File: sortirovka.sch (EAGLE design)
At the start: 37 parts, among them IC1 DS1307/PCF8583, U1 MAX3485CSA, X1 PI3-CONMINIBOARD, X10 MKDSN1,5/3-5,08, X3 MKDSN1,5/4-5,08, X4 MKDSN1,5/2-5,08, X6 22-23-2051

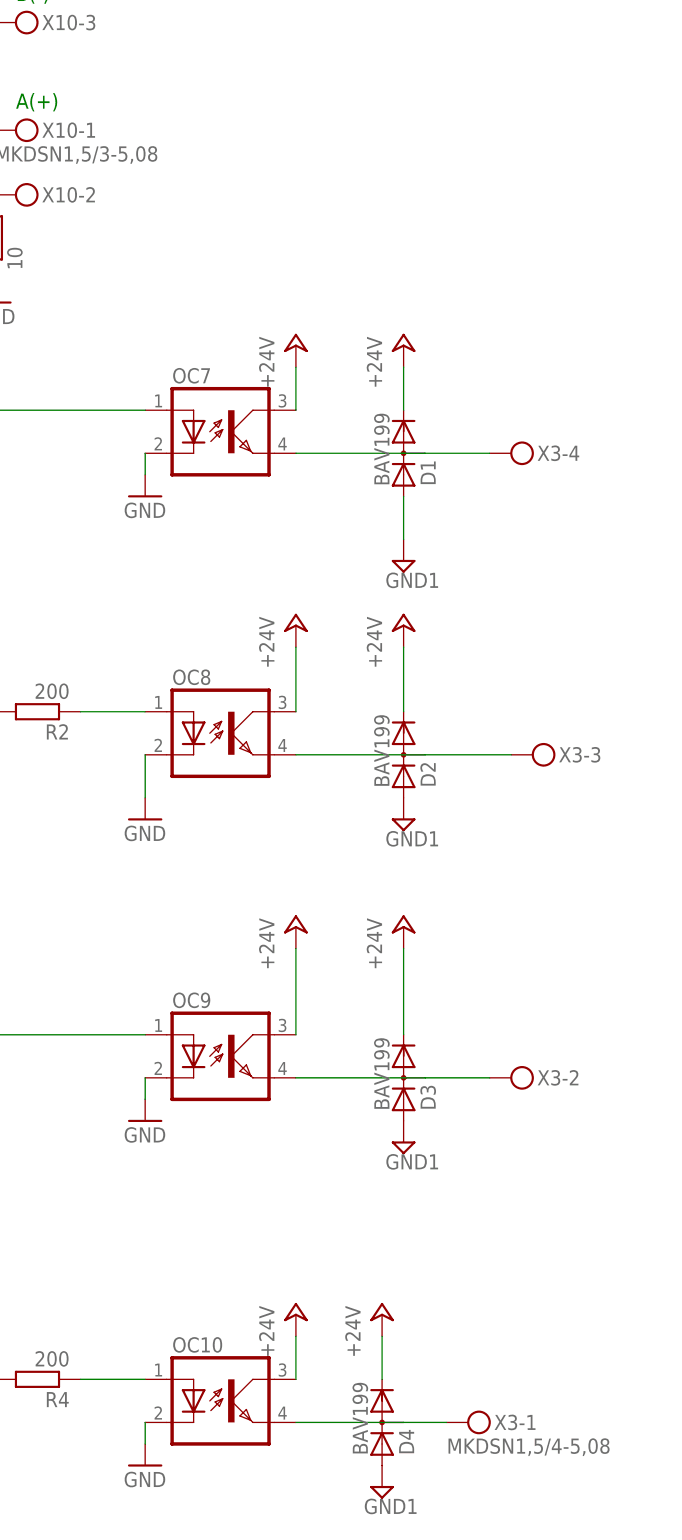
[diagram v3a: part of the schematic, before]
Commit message: current source for optocoupler, old design
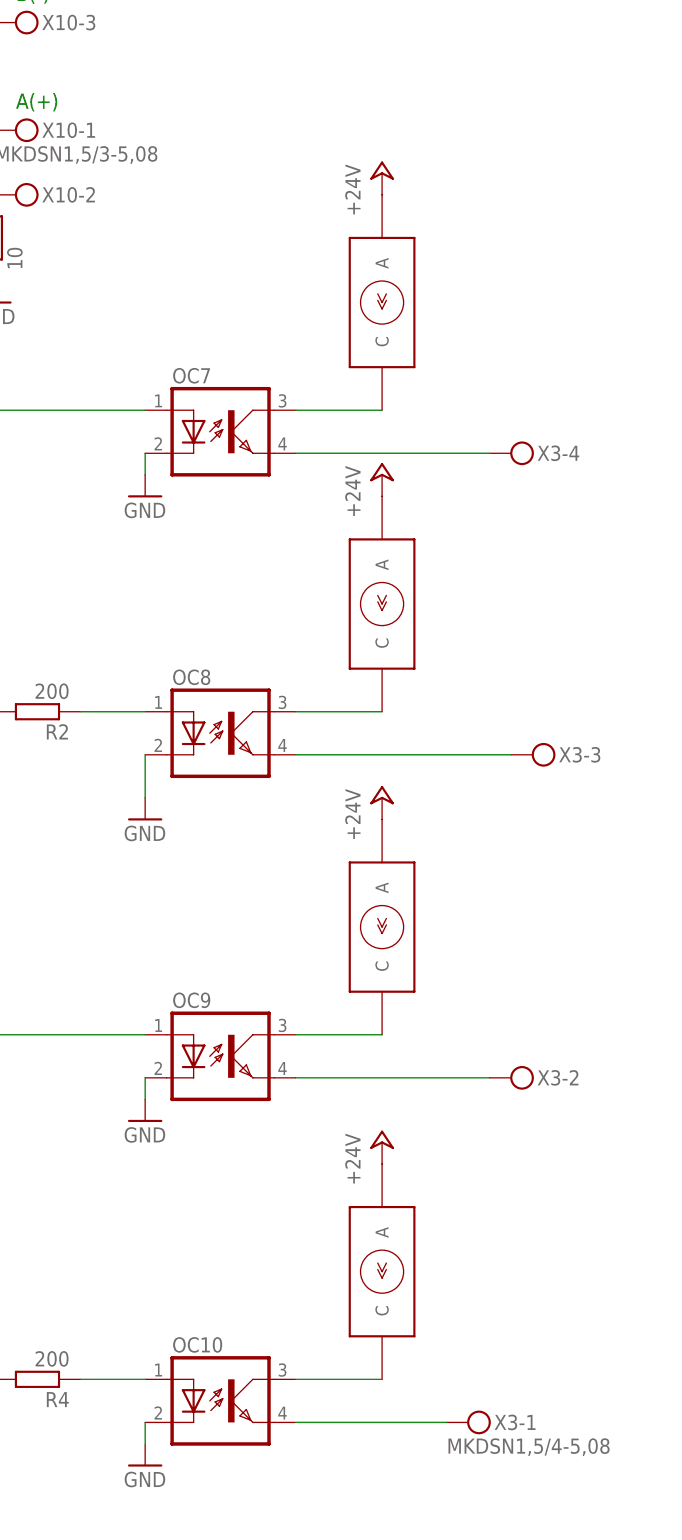
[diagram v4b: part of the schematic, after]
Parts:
- removed D1, D2, D3, D4: BAV199, MyLib:BAV199
- added U$1, U$2, U$4, U$5: NSI45020AT1GSOD-123, MyLib:NSI45020AT1GSOD-123
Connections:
- new net N$14: OC10.COL, U$5.C
- new net N$17: OC9.COL, U$1.C
- new net N$20: OC8.COL, U$4.C
- new net N$30: OC7.COL, U$2.C
- net +24V: now also U$1.A, U$2.A, U$4.A, U$5.A; no longer D1.C, D2.C, D3.C, D4.C, OC10.COL, OC7.COL, OC8.COL, OC9.COL
- net GND1: no longer D1.A, D2.A, D3.A, D4.A
- net N$10: no longer D4.AC
- net N$11: no longer D3.AC
- net N$12: no longer D2.AC
- net N$9: no longer D1.AC
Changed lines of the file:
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@@
 <part name="X4" library="con-phoenix-508" deviceset="MKDSN1,5/2-5,08" device=""/>
 <part name="P+2" library="supply1" deviceset="+24V" device=""/>
-<part name="SUPPLY1" library="supply2" deviceset="GND1" device=""/>
 <part name="SUPPLY5" library="supply2" deviceset="GND1" device=""/>
 <part name="OC7" library="MyLib" deviceset="SFH6106" device="REAL"/>
@@
 <part name="+3V6" library="supply1" deviceset="+3V3" device=""/>
 <part name="PWS1" library="MyLib" deviceset="TEN_3*" device="-1" technology="2410"/>
-<part name="D1" library="MyLib" deviceset="BAV199" device=""/>
-<part name="D2" library="MyLib" deviceset="BAV199" device=""/>
-<part name="D3" library="MyLib" deviceset="BAV199" device=""/>
-<part name="D4" library="MyLib" deviceset="BAV199" device=""/>
-<part name="P+1" library="supply1" deviceset="+24V" device=""/>
-<part name="P+7" library="supply1" deviceset="+24V" device=""/>
-<part name="P+8" library="supply1" deviceset="+24V" device=""/>
-<part name="P+9" library="supply1" deviceset="+24V" device=""/>
-<part name="SUPPLY2" library="supply2" deviceset="GND1" device=""/>
-<part name="SUPPLY3" library="supply2" deviceset="GND1" device=""/>
-<part name="SUPPLY4" library="supply2" deviceset="GND1" device=""/>
+<part name="U$1" library="MyLib" deviceset="NSI45020AT1G" device="SOD-123"/>
+<part name="U$2" library="MyLib" deviceset="NSI45020AT1G" device="SOD-123"/>
+<part name="U$4" library="MyLib" deviceset="NSI45020AT1G" device="SOD-123"/>
+<part name="U$5" library="MyLib" deviceset="NSI45020AT1G" device="SOD-123"/>
 </parts>
 <sheets>
@@
 <instance part="X4" gate="-2" x="147.32" y="144.78" rot="MR0"/>
 <instance part="P+2" gate="1" x="154.94" y="147.32" rot="MR0"/>
-<instance part="SUPPLY1" gate="G$1" x="345.44" y="10.16"/>
 <instance part="SUPPLY5" gate="G$1" x="167.64" y="129.54" rot="MR0"/>
 <instance part="OC7" gate="A" x="325.12" y="25.4"/>
 <instance part="GND2" gate="1" x="314.96" y="17.78"/>
-<instance part="P+3" gate="1" x="332.74" y="35.56"/>
+<instance part="P+3" gate="1" x="342.9" y="55.88"/>
 <instance part="OC8" gate="A" x="325.12" y="-10.16"/>
 <instance part="GND9" gate="1" x="314.96" y="-20.32"/>
-<instance part="P+4" gate="1" x="332.74" y="2.54"/>
+<instance part="P+4" gate="1" x="342.9" y="20.32"/>
 <instance part="OC9" gate="A" x="325.12" y="-48.26"/>
 <instance part="GND12" gate="1" x="314.96" y="-55.88"/>
-<instance part="P+5" gate="1" x="332.74" y="-33.02"/>
+<instance part="P+5" gate="1" x="342.9" y="-17.78"/>
 <instance part="OC10" gate="A" x="325.12" y="-88.9"/>
 <instance part="GND13" gate="1" x="314.96" y="-96.52"/>
-<instance part="P+6" gate="1" x="332.74" y="-78.74"/>
+<instance part="P+6" gate="1" x="342.9" y="-58.42"/>
 <instance part="GND24" gate="1" x="299.72" y="124.46"/>
 <instance part="C8" gate="G$1" x="279.4" y="132.08"/>
@@
 <instance part="+3V6" gate="G$1" x="68.58" y="81.28"/>
 <instance part="PWS1" gate="G$1" x="213.36" y="134.62"/>
-<instance part="D1" gate="G$1" x="345.44" y="22.86" rot="R270"/>
-<instance part="D2" gate="G$1" x="345.44" y="-12.7" rot="R270"/>
-<instance part="D3" gate="G$1" x="345.44" y="-50.8" rot="R270"/>
-<instance part="D4" gate="G$1" x="342.9" y="-91.44" rot="R270"/>
-<instance part="P+1" gate="1" x="342.9" y="-78.74"/>
-<instance part="P+7" gate="1" x="345.44" y="-33.02"/>
-<instance part="P+8" gate="1" x="345.44" y="2.54"/>
-<instance part="P+9" gate="1" x="345.44" y="35.56"/>
-<instance part="SUPPLY2" gate="G$1" x="345.44" y="-20.32"/>
-<instance part="SUPPLY3" gate="G$1" x="342.9" y="-99.06"/>
-<instance part="SUPPLY4" gate="G$1" x="345.44" y="-58.42"/>
+<instance part="U$1" gate="G$1" x="342.9" y="-33.02" rot="R270"/>
+<instance part="U$2" gate="G$1" x="342.9" y="40.64" rot="R270"/>
+<instance part="U$4" gate="G$1" x="342.9" y="5.08" rot="R270"/>
+<instance part="U$5" gate="G$1" x="342.9" y="-73.66" rot="R270"/>
 </instances>
 <busses>
@@
 <pinref part="OC10" gate="A" pin="EMIT"/>
 <pinref part="X3" gate="-1" pin="KL"/>
-<pinref part="D4" gate="G$1" pin="AC"/>
-<wire x1="350.52" y1="-91.44" x2="345.44" y2="-91.44" width="0.1524" layer="91"/>
-<wire x1="345.44" y1="-91.44" x2="332.74" y2="-91.44" width="0.1524" layer="91"/>
+<wire x1="350.52" y1="-91.44" x2="332.74" y2="-91.44" width="0.1524" layer="91"/>
 </segment>
 </net>
@@
 <pinref part="OC8" gate="A" pin="EMIT"/>
 <pinref part="X3" gate="-3" pin="KL"/>
-<pinref part="D2" gate="G$1" pin="AC"/>
-<wire x1="358.14" y1="-12.7" x2="347.98" y2="-12.7" width="0.1524" layer="91"/>
-<wire x1="347.98" y1="-12.7" x2="332.74" y2="-12.7" width="0.1524" layer="91"/>
+<wire x1="358.14" y1="-12.7" x2="332.74" y2="-12.7" width="0.1524" layer="91"/>
 </segment>
 </net>
@@
 </segment>
 <segment>
-<pinref part="OC7" gate="A" pin="COL"/>
+<pinref part="U$5" gate="G$1" pin="A"/>
+<pinref part="P+6" gate="1" pin="+24V"/>
+</segment>
+<segment>
+<pinref part="U$1" gate="G$1" pin="A"/>
+<pinref part="P+5" gate="1" pin="+24V"/>
+</segment>
+<segment>
+<pinref part="U$4" gate="G$1" pin="A"/>
+<pinref part="P+4" gate="1" pin="+24V"/>
+</segment>
+<segment>
+<pinref part="U$2" gate="G$1" pin="A"/>
 <pinref part="P+3" gate="1" pin="+24V"/>
-<wire x1="332.74" y1="27.94" x2="332.74" y2="33.02" width="0.1524" layer="91"/>
-</segment>
-<segment>
-<pinref part="OC8" gate="A" pin="COL"/>
-<pinref part="P+4" gate="1" pin="+24V"/>
-<wire x1="332.74" y1="-7.62" x2="332.74" y2="0" width="0.1524" layer="91"/>
-</segment>
-<segment>
-<pinref part="OC9" gate="A" pin="COL"/>
-<wire x1="332.74" y1="-45.72" x2="332.74" y2="-35.56" width="0.1524" layer="91"/>
-<pinref part="P+5" gate="1" pin="+24V"/>
-</segment>
-<segment>
-<pinref part="OC10" gate="A" pin="COL"/>
-<wire x1="332.74" y1="-86.36" x2="332.74" y2="-81.28" width="0.1524" layer="91"/>
-<pinref part="P+6" gate="1" pin="+24V"/>
-</segment>
-<segment>
-<pinref part="D4" gate="G$1" pin="C"/>
-<pinref part="P+1" gate="1" pin="+24V"/>
-<wire x1="342.9" y1="-86.36" x2="342.9" y2="-81.28" width="0.1524" layer="91"/>
-</segment>
-<segment>
-<pinref part="D3" gate="G$1" pin="C"/>
-<pinref part="P+7" gate="1" pin="+24V"/>
-<wire x1="345.44" y1="-45.72" x2="345.44" y2="-35.56" width="0.1524" layer="91"/>
-</segment>
-<segment>
-<pinref part="D2" gate="G$1" pin="C"/>
-<pinref part="P+8" gate="1" pin="+24V"/>
-<wire x1="345.44" y1="-7.62" x2="345.44" y2="0" width="0.1524" layer="91"/>
-</segment>
-<segment>
-<pinref part="D1" gate="G$1" pin="C"/>
-<pinref part="P+9" gate="1" pin="+24V"/>
-<wire x1="345.44" y1="27.94" x2="345.44" y2="33.02" width="0.1524" layer="91"/>
 </segment>
 </net>
@@
 <junction x="193.04" y="129.54"/>
 </segment>
-<segment>
-<pinref part="D3" gate="G$1" pin="A"/>
-<pinref part="SUPPLY4" gate="G$1" pin="GND1"/>
-</segment>
-<segment>
-<pinref part="D4" gate="G$1" pin="A"/>
-<pinref part="SUPPLY3" gate="G$1" pin="GND1"/>
-</segment>
-<segment>
-<pinref part="D2" gate="G$1" pin="A"/>
-<pinref part="SUPPLY2" gate="G$1" pin="GND1"/>
-</segment>
-<segment>
-<pinref part="D1" gate="G$1" pin="A"/>
-<pinref part="SUPPLY1" gate="G$1" pin="GND1"/>
-<wire x1="345.44" y1="17.78" x2="345.44" y2="12.7" width="0.1524" layer="91"/>
-</segment>
 </net>
 <net name="N$15" class="0">
@@
 <segment>
 <pinref part="X3" gate="-4" pin="KL"/>
-<pinref part="D1" gate="G$1" pin="AC"/>
-<wire x1="355.6" y1="22.86" x2="347.98" y2="22.86" width="0.1524" layer="91"/>
 <pinref part="OC7" gate="A" pin="EMIT"/>
-<wire x1="347.98" y1="22.86" x2="332.74" y2="22.86" width="0.1524" layer="91"/>
+<wire x1="355.6" y1="22.86" x2="332.74" y2="22.86" width="0.1524" layer="91"/>
 </segment>
 </net>
@@
 <segment>
 <pinref part="X3" gate="-2" pin="KL"/>
-<pinref part="D3" gate="G$1" pin="AC"/>
-<wire x1="355.6" y1="-50.8" x2="347.98" y2="-50.8" width="0.1524" layer="91"/>
 <pinref part="OC9" gate="A" pin="EMIT"/>
-<wire x1="347.98" y1="-50.8" x2="332.74" y2="-50.8" width="0.1524" layer="91"/>
+<wire x1="355.6" y1="-50.8" x2="332.74" y2="-50.8" width="0.1524" layer="91"/>
 </segment>
 </net>
@@
 </segment>
 </net>
+<net name="N$14" class="0">
+<segment>
+<pinref part="OC10" gate="A" pin="COL"/>
+<pinref part="U$5" gate="G$1" pin="C"/>
+<wire x1="332.74" y1="-86.36" x2="342.9" y2="-86.36" width="0.1524" layer="91"/>
+</segment>
+</net>
+<net name="N$17" class="0">
+<segment>
+<pinref part="OC9" gate="A" pin="COL"/>
+<pinref part="U$1" gate="G$1" pin="C"/>
+<wire x1="332.74" y1="-45.72" x2="342.9" y2="-45.72" width="0.1524" layer="91"/>
+</segment>
+</net>
+<net name="N$20" class="0">
+<segment>
+<pinref part="OC8" gate="A" pin="COL"/>
+<pinref part="U$4" gate="G$1" pin="C"/>
+<wire x1="332.74" y1="-7.62" x2="342.9" y2="-7.62" width="0.1524" layer="91"/>
+</segment>
+</net>
+<net name="N$30" class="0">
+<segment>
+<pinref part="OC7" gate="A" pin="COL"/>
+<pinref part="U$2" gate="G$1" pin="C"/>
+<wire x1="332.74" y1="27.94" x2="342.9" y2="27.94" width="0.1524" layer="91"/>
+</segment>
+</net>

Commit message: wip
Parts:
- removed R15: 120, rcl:R-EU_0207/10
- removed X10: MKDSN1,5/3-5,08, con-phoenix-508:MKDSN1,5/3-5,08
- removed X6: 22-23-2051, con-molex:22-23-2051
- added IC2: PCF8574T, MyLib:PCF8574T
- added IC3: DS1307/PCF8583, MyLib:DS1307/PCF8583
- added LCD1: LCD_2X16_SIL, lcd_2x16_led_backlight:LCD_2X16_SIL
- added LCD2: LCD_128X64-NO_RESTRICTS, lcd_128x64_led_backlight:LCD_128X64-NO_RESTRICTS
- added R12: 200, rcl:R-EU_R0805
- added X2: PI3-CONMINIBOARD, MyLib:PI3-CONMINIBOARD
- added X5: MKDSN1,5/4-5,08, con-phoenix-508:MKDSN1,5/4-5,08
- IC1: value DS1307/PCF8583 -> PCF8574T; device MyLib:DS1307/PCF8583 -> MyLib:PCF8574T
- R1, R2: value 200 -> 3k3
- R10: value 3k3 -> 10
- R11: value 3k3 -> 200
- R3, R4: value 200 -> 1k5
- R5, R6: value 1k5 -> 15
- R7: value 15 -> 200
- R8: value 15 -> 120; device rcl:R-EU_R0805 -> rcl:R-EU_0207/10
- R9: value 10 -> 200
- X1: value PI3-CONMINIBOARD -> 22-23-2051; device MyLib:PI3-CONMINIBOARD -> con-molex:22-23-2051
- X3: value MKDSN1,5/4-5,08 -> MKDSN1,5/2-5,08; device con-phoenix-508:MKDSN1,5/4-5,08 -> con-phoenix-508:MKDSN1,5/2-5,08
- X4: value MKDSN1,5/2-5,08 -> MKDSN1,5/3-5,08; device con-phoenix-508:MKDSN1,5/2-5,08 -> con-phoenix-508:MKDSN1,5/3-5,08
- renumbered C10 to C2, C8 to C4, C9 to C3, OC10 to OC4, OC7 to OC1, OC8 to OC2, OC9 to OC3, U$1 to D4, U$2 to D2, U$3 to D1, U$4 to D3, U$5 to D5
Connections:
- net +24V: now also X3-2.KL; no longer X4-2.KL
- net +3V3: now also IC1.A0, IC1.VDD, IC2.VDD, IC3.VCC, R1.2, R2.2, R4.1, X2.3.3V@1, X2.3.3V@2; no longer IC1.VCC, R10.2, R11.2, R6.1, X1.3.3V@1, X1.3.3V@2
- net A+: now also R4.2, R6.1; no longer R6.2, R8.1
- net B-: now also R3.1; no longer R7.1
- net GND: now also IC1.A1, IC1.A2, IC1.VSS, IC2.A0, IC2.A1, IC2.A2, IC2.VSS, IC3.GND, R10.1, R3.2, X1-5.S, X2.GND@1, X2.GND@2, X2.GND@3, X2.GND@4, X2.GND@5, X2.GND@6, X2.GND@7, X2.GND@8; no longer IC1.GND, R5.2, R9.1, X1.GND@1, X1.GND@2, X1.GND@3, X1.GND@4, X1.GND@5, X1.GND@6, X1.GND@7, X1.GND@8, X6-5.S
- net GND1: now also X3-1.KL; no longer X4-1.KL
- net MISO: now also X1-3.S, X2.GPIO09; no longer X1.GPIO09, X6-3.S
- net MOSI: now also X1-4.S, X2.GPIO10; no longer X1.GPIO10, X6-4.S
- net N$1: now also R7.2, X2.GPIO20; no longer R3.2, X1.GPIO20
- net N$10: now also X5-1.KL; no longer X3-1.KL
- net N$11: now also X5-2.KL; no longer X3-2.KL
- net N$12: now also X5-3.KL; no longer X3-3.KL
- net N$13: now also R5.2, R8.2, X4-3.KL; no longer R15.2, R7.2, X10-3.KL
- net N$15: now also R9.1; no longer R1.1
- net N$18: now also R11.1; no longer R2.1
- net N$19: now also R7.1; no longer R3.1
- net N$2: now also R12.2, X2.GPIO21; no longer R4.2, X1.GPIO21
- net N$28: now also X2.+5V@1, X2.+5V@2; no longer X1.+5V@1, X1.+5V@2
- net N$29: now also R12.1; no longer R4.1
- net N$3: now also IC3.VBAT; no longer IC1.VBAT
- net N$4: now also IC3.X1; no longer IC1.X1
- net N$46: now also R6.2, R8.1, X4-1.KL; no longer R15.1, R8.2, X10-1.KL
- net N$5: now also R10.2, X4-2.KL; no longer R9.2, X10-2.KL
- net N$6: now also R9.2, X2.GPIO12; no longer R1.2, X1.GPIO12
- net N$7: now also R11.2, X2.GPIO16; no longer R2.2, X1.GPIO16
- net N$8: now also IC3.X2; no longer IC1.X2
- net N$9: now also X5-4.KL; no longer X3-4.KL
- net R/E: now also X2.GPIO18; no longer X1.GPIO18
- net RX: now also X2.GPIO15; no longer X1.GPIO15
- net SCL: now also IC2.SCL, IC3.SCL, R1.1, X2.GPIO03; no longer R10.1, X1.GPIO03
- net SDA: now also IC2.SDA, IC3.SDA, R2.1, X2.GPIO02; no longer R11.1, X1.GPIO02
- net SPI0: now also X1-2.S, X2.GPIO08; no longer X1.GPIO08, X6-2.S
- net SPI1: now also X2.GPIO07; no longer X1.GPIO07
- net SPI_CLK: now also X1-1.S, X2.GPIO11; no longer X1.GPIO11, X6-1.S
- net TX: now also X2.GPIO14; no longer X1.GPIO14
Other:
- moved on the sheet: R1, R10, R11, R2, R3, R4, R5, R6, R7, R8, R9, X3-1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
